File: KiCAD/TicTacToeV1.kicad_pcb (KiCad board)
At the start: 2 copper layers, 64 x 87 mm, 34 parts, among them U1 74HC165, U2 74HC165, U3 MAX7219

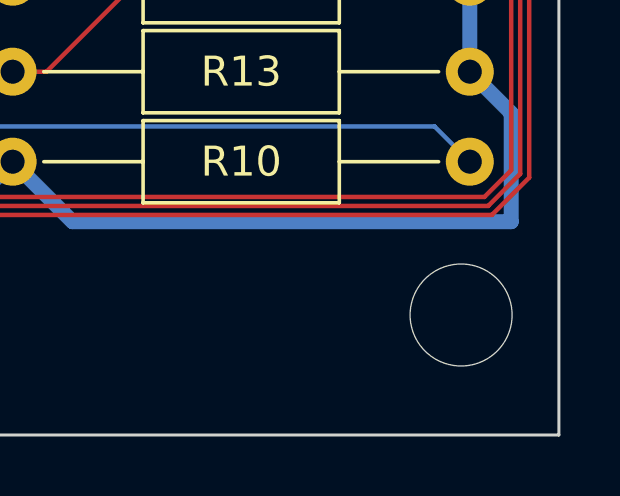
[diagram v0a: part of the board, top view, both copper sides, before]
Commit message: Added case design.
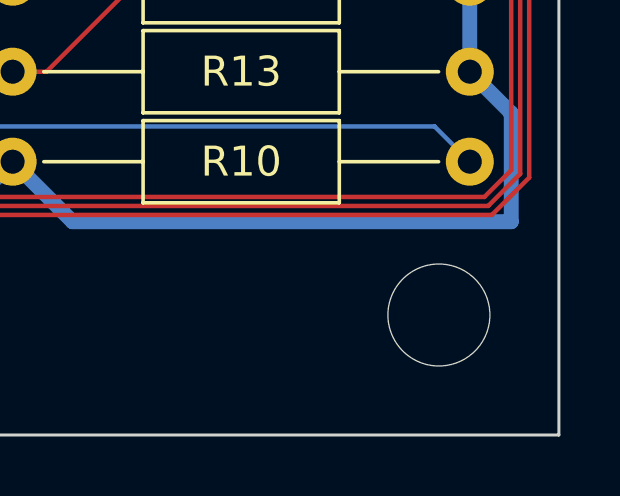
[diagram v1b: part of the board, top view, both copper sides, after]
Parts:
- moved H4 0.74 mm to (78.0, 99.0)
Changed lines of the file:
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@@
   (net 82 "Net-(S1-PadA2)")
   (footprint "TicTacToeV1:M3-NPTH" (layer "F.Cu")
-    (at 78.74 99)
+    (at 78 99)
     (property "Sheetfile" "TicTacToeV1.kicad_sch")
     (property "Sheetname" "")
@@
   (gr_line (start 82 103) (end 18 103) (layer "Edge.Cuts") (width 0.1))
   (gr_line (start 18 16) (end 82 16) (layer "Edge.Cuts") (width 0.1))
+  (dimension (type aligned) (layer "Edge.Cuts")
+    (pts (xy 82 16) (xy 82 103))
+    (height -6.9)
+    (gr_text "87 mm" (at 87.75 59.5 90) (layer "Edge.Cuts")
+      (effects (font (size 1 1) (thickness 0.15)))
+    )
+    (format (units 3) (units_format 1) (precision 4) suppress_zeroes)
+    (style (thickness 0.1) (arrow_length 1.27) (text_position_mode 0) (extension_height 0.58642) (extension_offset 0.5) keep_text_aligned)
+  )
+  (dimension (type aligned) (layer "Edge.Cuts")
+    (pts (xy 22 99) (xy 18 99))
+    (height -6.4)
+    (gr_text "4 mm" (at 24.5 105.5) (layer "Edge.Cuts")
+      (effects (font (size 1 1) (thickness 0.15)))
+    )
+    (format (units 3) (units_format 1) (precision 4) suppress_zeroes)
+    (style (thickness 0.1) (arrow_length 1.27) (text_position_mode 2) (extension_height 0.58642) (extension_offset 0.5) keep_text_aligned)
+  )
+  (dimension (type aligned) (layer "Edge.Cuts")
+    (pts (xy 18 103) (xy 82 103))
+    (height 6.22)
+    (gr_text "64 mm" (at 50 108.07) (layer "Edge.Cuts")
+      (effects (font (size 1 1) (thickness 0.15)))
+    )
+    (format (units 3) (units_format 1) (precision 4) suppress_zeroes)
+    (style (thickness 0.1) (arrow_length 1.27) (text_position_mode 0) (extension_height 0.58642) (extension_offset 0.5) keep_text_aligned)
+  )
+  (dimension (type aligned) (layer "Edge.Cuts")
+    (pts (xy 22 99) (xy 22 103))
+    (height -5.5)
+    (gr_text "4 mm" (at 29.2 100.5 90) (layer "Edge.Cuts")
+      (effects (font (size 1 1) (thickness 0.15)))
+    )
+    (format (units 3) (units_format 1) (precision 4) suppress_zeroes)
+    (style (thickness 0.1) (arrow_length 1.27) (text_position_mode 2) (extension_height 0.58642) (extension_offset 0.5) keep_text_aligned)
+  )
   (segment (start 55.31 65.865) (end 57.96 68.515) (width 0.5) (layer "B.Cu") (net 4))
   (segment (start 31.58 29.56) (end 31.58 32.205) (width 0.5) (layer "B.Cu") (net 4))
